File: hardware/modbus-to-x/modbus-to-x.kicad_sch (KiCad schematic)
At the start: 23 parts, among them SW1 SW_Push, SW2 SW_Push, U1 AMS1117-3.3, U2 LM7805_TO220, U3 MAX3485, U4 ESP32-WROOM-32D, U5 AT24CS64-XHM, U6 AT24CS64-XHM

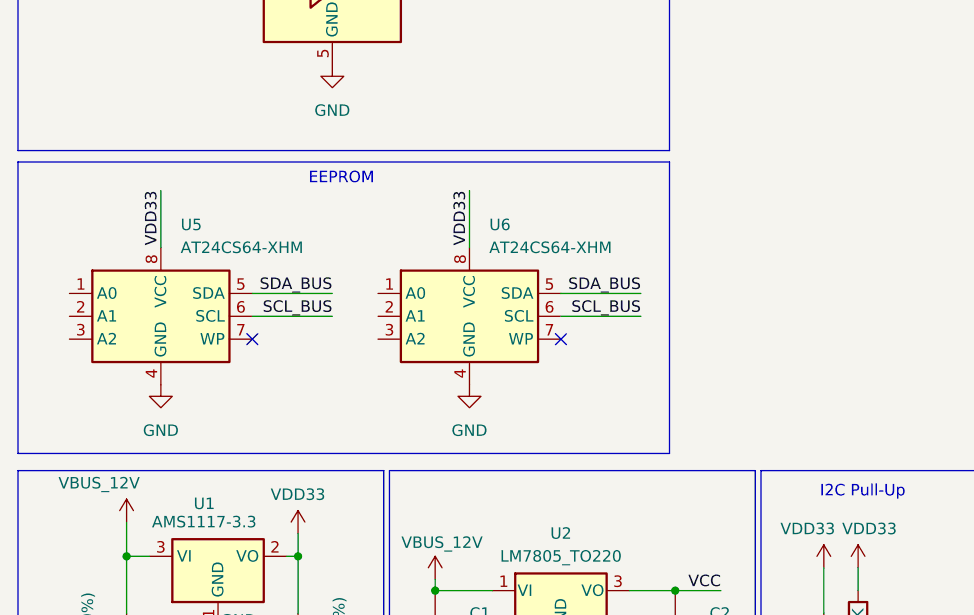
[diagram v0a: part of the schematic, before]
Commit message: hardwiring address pins in eeproms
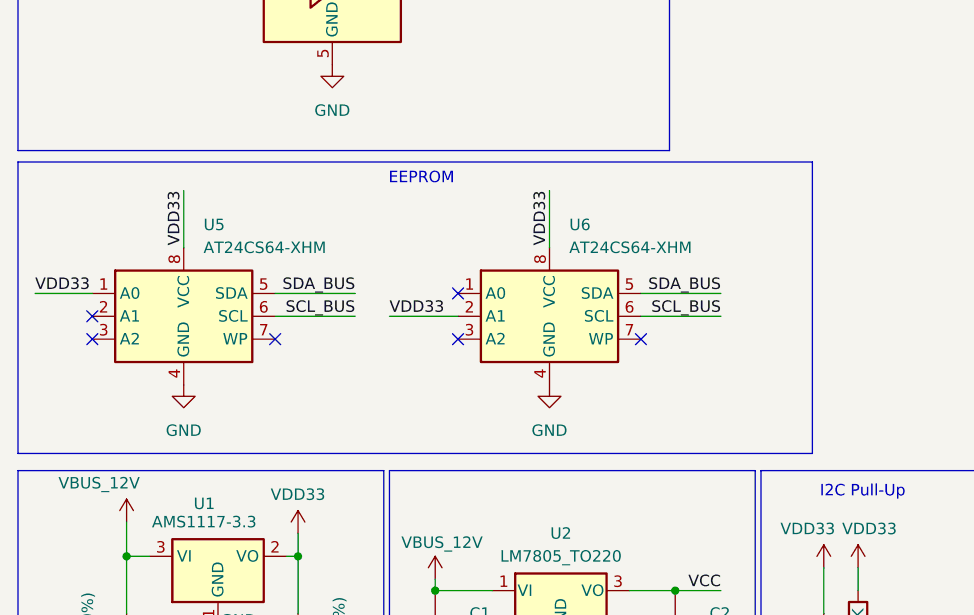
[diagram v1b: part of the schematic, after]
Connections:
- net VDD33: now also U5.1 (A0), U6.2 (A1)
- no-connect marks 10 -> 14
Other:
- moved on the sheet: U5, U6
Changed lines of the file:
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@@
 	)
 	(no_connect
-		(at 40.64 147.32)
+		(at 22.86 147.32)
+	)
+	(no_connect
+		(at 43.18 147.32)
 	)
 	(no_connect
@@
 	)
 	(no_connect
+		(at 22.86 144.78)
+	)
+	(no_connect
 		(at 240.03 72.39)
 	)
 	(no_connect
+		(at 63.5 147.32)
+	)
+	(no_connect
 		(at 240.03 77.47)
 	)
 	(no_connect
+		(at 63.5 142.24)
+	)
+	(no_connect
 		(at 240.03 69.85)
 	)
@@
 	)
 	(no_connect
-		(at 74.93 147.32)
+		(at 83.82 147.32)
 	)
 	(wire
@@
 	(wire
 		(pts
-			(xy 49.53 142.24) (xy 40.64 142.24)
+			(xy 52.07 142.24) (xy 43.18 142.24)
 		)
 		(stroke
@@
 	(wire
 		(pts
-			(xy 83.82 144.78) (xy 74.93 144.78)
+			(xy 92.71 144.78) (xy 83.82 144.78)
 		)
 		(stroke
@@
 	(wire
 		(pts
-			(xy 64.77 130.81) (xy 64.77 137.16)
+			(xy 73.66 130.81) (xy 73.66 137.16)
 		)
 		(stroke
@@
 	(wire
 		(pts
-			(xy 30.48 130.81) (xy 30.48 137.16)
+			(xy 33.02 130.81) (xy 33.02 137.16)
 		)
 		(stroke
@@
 	(wire
 		(pts
+			(xy 55.88 144.78) (xy 63.5 144.78)
+		)
+		(stroke
+			(width 0)
+			(type default)
+		)
+	)
+	(wire
+		(pts
 			(xy 198.12 102.87) (xy 198.12 97.79)
 		)
@@
 	(wire
 		(pts
-			(xy 49.53 144.78) (xy 40.64 144.78)
+			(xy 52.07 144.78) (xy 43.18 144.78)
 		)
 		(stroke
@@
 	(wire
 		(pts
-			(xy 83.82 142.24) (xy 74.93 142.24)
+			(xy 92.71 142.24) (xy 83.82 142.24)
 		)
 		(stroke
@@
 		)
 	)
+	(wire
+		(pts
+			(xy 16.51 142.24) (xy 22.86 142.24)
+		)
+		(stroke
+			(width 0)
+			(type default)
+		)
+	)
 	(rectangle
 		(start 152.4 12.7)
@@
 	(rectangle
 		(start 14.605 127.635)
-		(end 86.995 160.02)
+		(end 102.87 160.02)
 		(stroke
 			(width 0)
@@
 	(text "EEPROM\n"
 		(exclude_from_sim no)
-		(at 50.546 129.54 0)
+		(at 59.436 129.54 0)
 		(effects
 			(font
@@
 	)
 	(label "VDD33"
-		(at 30.48 130.81 270)
+		(at 33.02 130.81 270)
 		(fields_autoplaced yes)
 		(effects
@@
 	)
 	(label "SCL_BUS"
-		(at 83.82 144.78 180)
+		(at 92.71 144.78 180)
 		(fields_autoplaced yes)
 		(effects
@@
 	)
 	(label "SCL_BUS"
-		(at 49.53 144.78 180)
+		(at 52.07 144.78 180)
 		(fields_autoplaced yes)
 		(effects
@@
 	)
 	(label "SDA_BUS"
-		(at 83.82 142.24 180)
+		(at 92.71 142.24 180)
 		(fields_autoplaced yes)
 		(effects
@@
 	)
 	(label "VDD33"
-		(at 64.77 130.81 270)
+		(at 73.66 130.81 270)
 		(fields_autoplaced yes)
 		(effects
@@
 	)
 	(label "SDA_BUS"
-		(at 49.53 142.24 180)
+		(at 52.07 142.24 180)
 		(fields_autoplaced yes)
 		(effects
@@
 		)
 	)
+	(label "VDD33"
+		(at 55.88 144.78 0)
+		(fields_autoplaced yes)
+		(effects
+			(font
+				(size 1.27 1.27)
+			)
+			(justify left bottom)
+		)
+	)
+	(label "VDD33"
+		(at 16.51 142.24 0)
+		(fields_autoplaced yes)
+		(effects
+			(font
+				(size 1.27 1.27)
+			)
+			(justify left bottom)
+		)
+	)
 	(label "RS485_RE"
 		(at 27.94 99.06 0)
@@
 	(symbol
 		(lib_id "power:GND")
-		(at 64.77 152.4 0)
+		(at 73.66 152.4 0)
 		(unit 1)
 		(exclude_from_sim no)
@@
 		(fields_autoplaced yes)
 		(property "Reference" "#PWR019"
-			(at 64.77 158.75 0)
+			(at 73.66 158.75 0)
 			(effects
 				(font
@@
 		)
 		(property "Value" "GND"
-			(at 64.77 157.48 0)
+			(at 73.66 157.48 0)
 			(effects
 				(font
@@
 		)
 		(property "Footprint" ""
-			(at 64.77 152.4 0)
+			(at 73.66 152.4 0)
 			(effects
 				(font
@@
 		)
 		(property "Datasheet" ""
-			(at 64.77 152.4 0)
+			(at 73.66 152.4 0)
 			(effects
 				(font
@@
 		)
 		(property "Description" "Power symbol creates a global label with name \"GND\" , ground"
-			(at 64.77 152.4 0)
+			(at 73.66 152.4 0)
 			(effects
 				(font
@@
 	(symbol
 		(lib_id "power:GND")
-		(at 30.48 152.4 0)
+		(at 33.02 152.4 0)
 		(unit 1)
 		(exclude_from_sim no)
@@
 		(fields_autoplaced yes)
 		(property "Reference" "#PWR018"
-			(at 30.48 158.75 0)
+			(at 33.02 158.75 0)
 			(effects
 				(font
@@
 		)
 		(property "Value" "GND"
-			(at 30.48 157.48 0)
+			(at 33.02 157.48 0)
 			(effects
 				(font
@@
 		)
 		(property "Footprint" ""
-			(at 30.48 152.4 0)
+			(at 33.02 152.4 0)
 			(effects
 				(font
@@
 		)
 		(property "Datasheet" ""
-			(at 30.48 152.4 0)
+			(at 33.02 152.4 0)
 			(effects
 				(font
@@
 		)
 		(property "Description" "Power symbol creates a global label with name \"GND\" , ground"
-			(at 30.48 152.4 0)
+			(at 33.02 152.4 0)
 			(effects
 				(font
@@
 	(symbol
 		(lib_id "Memory_EEPROM:AT24CS64-XHM")
-		(at 30.48 144.78 0)
+		(at 33.02 144.78 0)
 		(unit 1)
 		(exclude_from_sim no)
@@
 		(fields_autoplaced yes)
 		(property "Reference" "U5"
-			(at 32.6741 134.62 0)
+			(at 35.2141 134.62 0)
 			(effects
 				(font
@@
 		)
 		(property "Value" "AT24CS64-XHM"
-			(at 32.6741 137.16 0)
+			(at 35.2141 137.16 0)
 			(effects
 				(font
@@
 		)
 		(property "Footprint" "Package_SO:TSSOP-8_4.4x3mm_P0.65mm"
-			(at 30.48 144.78 0)
+			(at 33.02 144.78 0)
 			(effects
 				(font
@@
 		)
 		(property "Datasheet" "http://ww1.microchip.com/downloads/en/DeviceDoc/Atmel-8870-SEEPROM-AT24CS64-Datasheet.pdf"
-			(at 30.48 144.78 0)
+			(at 33.02 144.78 0)
 			(effects
 				(font
@@
 		)
 		(property "Description" "I2C Serial EEPROM, 64Kb (8192x8) with Unique Serial Number, TSSOP8"
-			(at 30.48 144.78 0)
+			(at 33.02 144.78 0)
 			(effects
 				(font
@@
 	(symbol
 		(lib_id "Memory_EEPROM:AT24CS64-XHM")
-		(at 64.77 144.78 0)
+		(at 73.66 144.78 0)
 		(unit 1)
 		(exclude_from_sim no)
@@
 		(fields_autoplaced yes)
 		(property "Reference" "U6"
-			(at 66.9641 134.62 0)
+			(at 75.8541 134.62 0)
 			(effects
 				(font
@@
 		)
 		(property "Value" "AT24CS64-XHM"
-			(at 66.9641 137.16 0)
+			(at 75.8541 137.16 0)
 			(effects
 				(font
@@
 		)
 		(property "Footprint" "Package_SO:TSSOP-8_4.4x3mm_P0.65mm"
-			(at 64.77 144.78 0)
+			(at 73.66 144.78 0)
 			(effects
 				(font
@@
 		)
 		(property "Datasheet" "http://ww1.microchip.com/downloads/en/DeviceDoc/Atmel-8870-SEEPROM-AT24CS64-Datasheet.pdf"
-			(at 64.77 144.78 0)
+			(at 73.66 144.78 0)
 			(effects
 				(font
@@
 		)
 		(property "Description" "I2C Serial EEPROM, 64Kb (8192x8) with Unique Serial Number, TSSOP8"
-			(at 64.77 144.78 0)
+			(at 73.66 144.78 0)
 			(effects
 				(font

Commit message: new power circuit WIP
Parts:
- added C10: 0.1uF, Capacitor_SMD:C_0402_1005Metric_Pad0.74x0.62mm_HandSolder, symbol Device:C
- added C11: 4.7uF, Capacitor_SMD:C_0402_1005Metric_Pad0.74x0.62mm_HandSolder, symbol Device:C
- added C12: 47uF, ~, symbol SparkFun-Capacitor:C_Polarized
- added D2: MBR0530, Diode_SMD:D_SOD-123, symbol Diode:MBR0530
- added L1: 5.5uH, SparkFun-Capacitor:C_0805_2012Metric, symbol SparkFun-Coil:L
- added R6, R8, R9: 10K, Resistor_SMD:R_0805_2012Metric_Pad1.20x1.40mm_HandSolder, symbol Device:R
- added R7: 23.2K, Resistor_SMD:R_0805_2012Metric_Pad1.20x1.40mm_HandSolder, symbol Device:R
- added U7: LMR14020SQDPRTQ1, DPR0010A, symbol LMR14020SQDPRTQ1:LMR14020SQDPRTQ1
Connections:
- net GND: now also C11.1, C12.2, D2.2 (A), R7.1, U7.11 (PAD), U7.9 (GND)
- net VBUS_12V: no longer C8.1, U1.3 (VI)
- net PGOOD: now reaches U4.16 (IO13)
- net PGOOD: now also R6.1
- new net: R6.2, U7.8 (PGOOD)
- new net: C10.2, U7.1 (BOOT)
- new net: D2.1 (K), L1.1, U7.10 (SW)
- new net: R7.2, U7.5 (RT_SYNC)
- new net: C11.2, U7.6 (SS)
- new net: R9.1, U7.7 (FB)
- new net: R8.2, R9.2
- new net VCC5: C12.1, C8.1, L1.2, R8.1, U1.3 (VI)

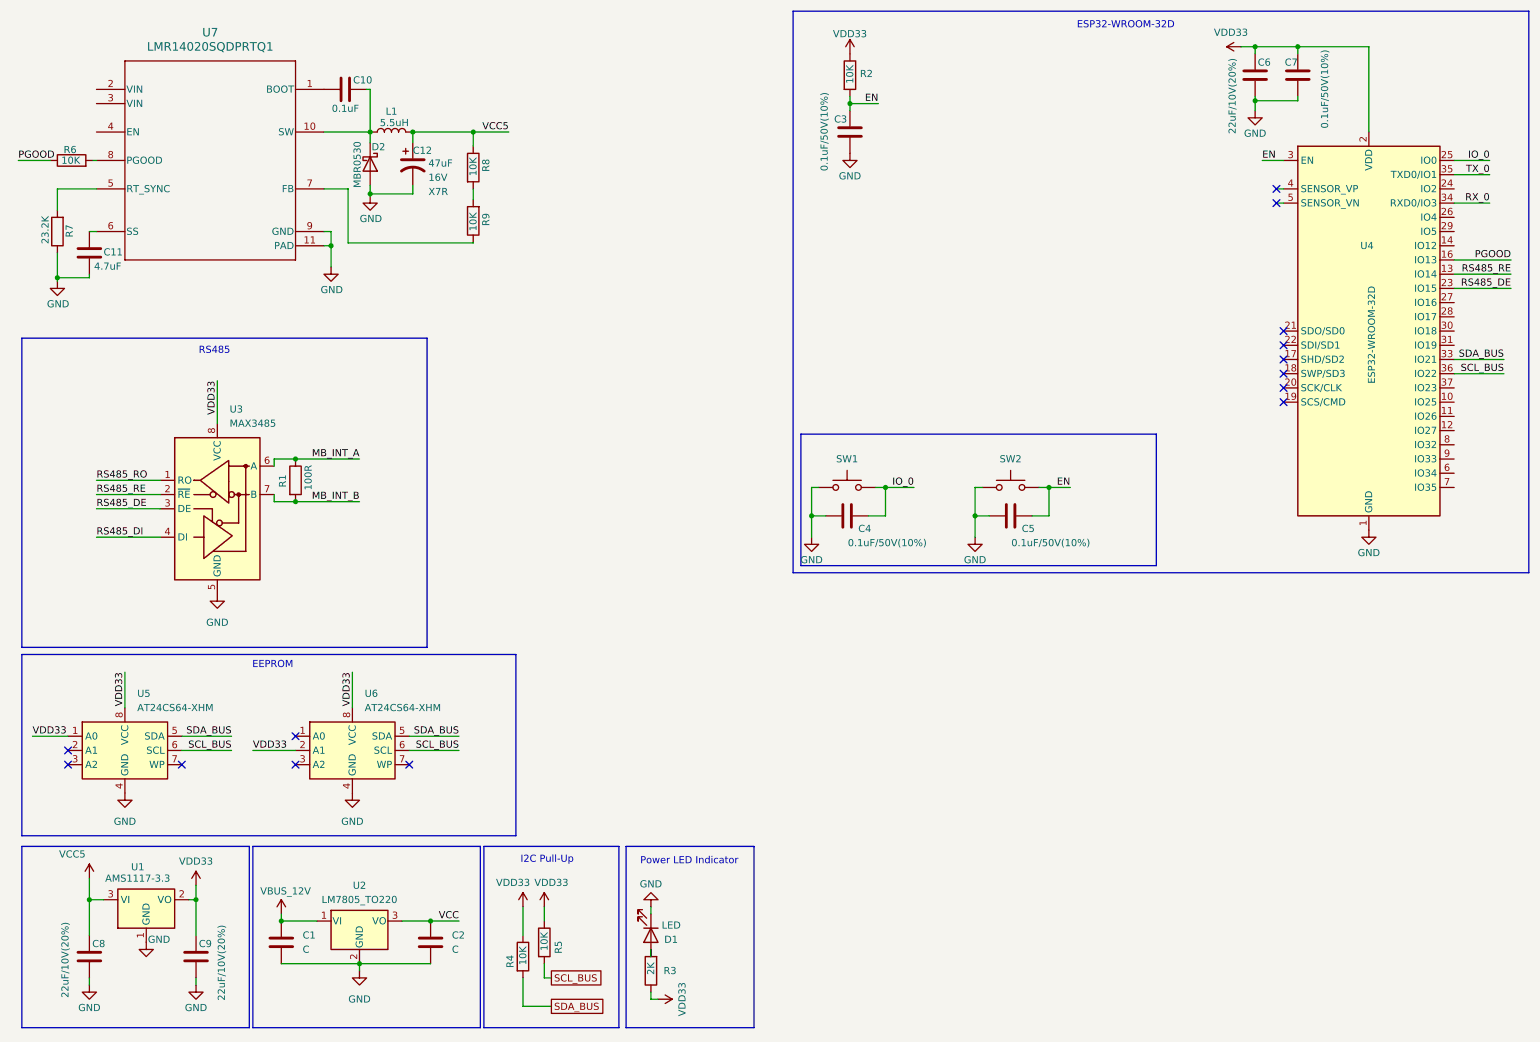
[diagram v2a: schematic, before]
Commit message: fixed warnings
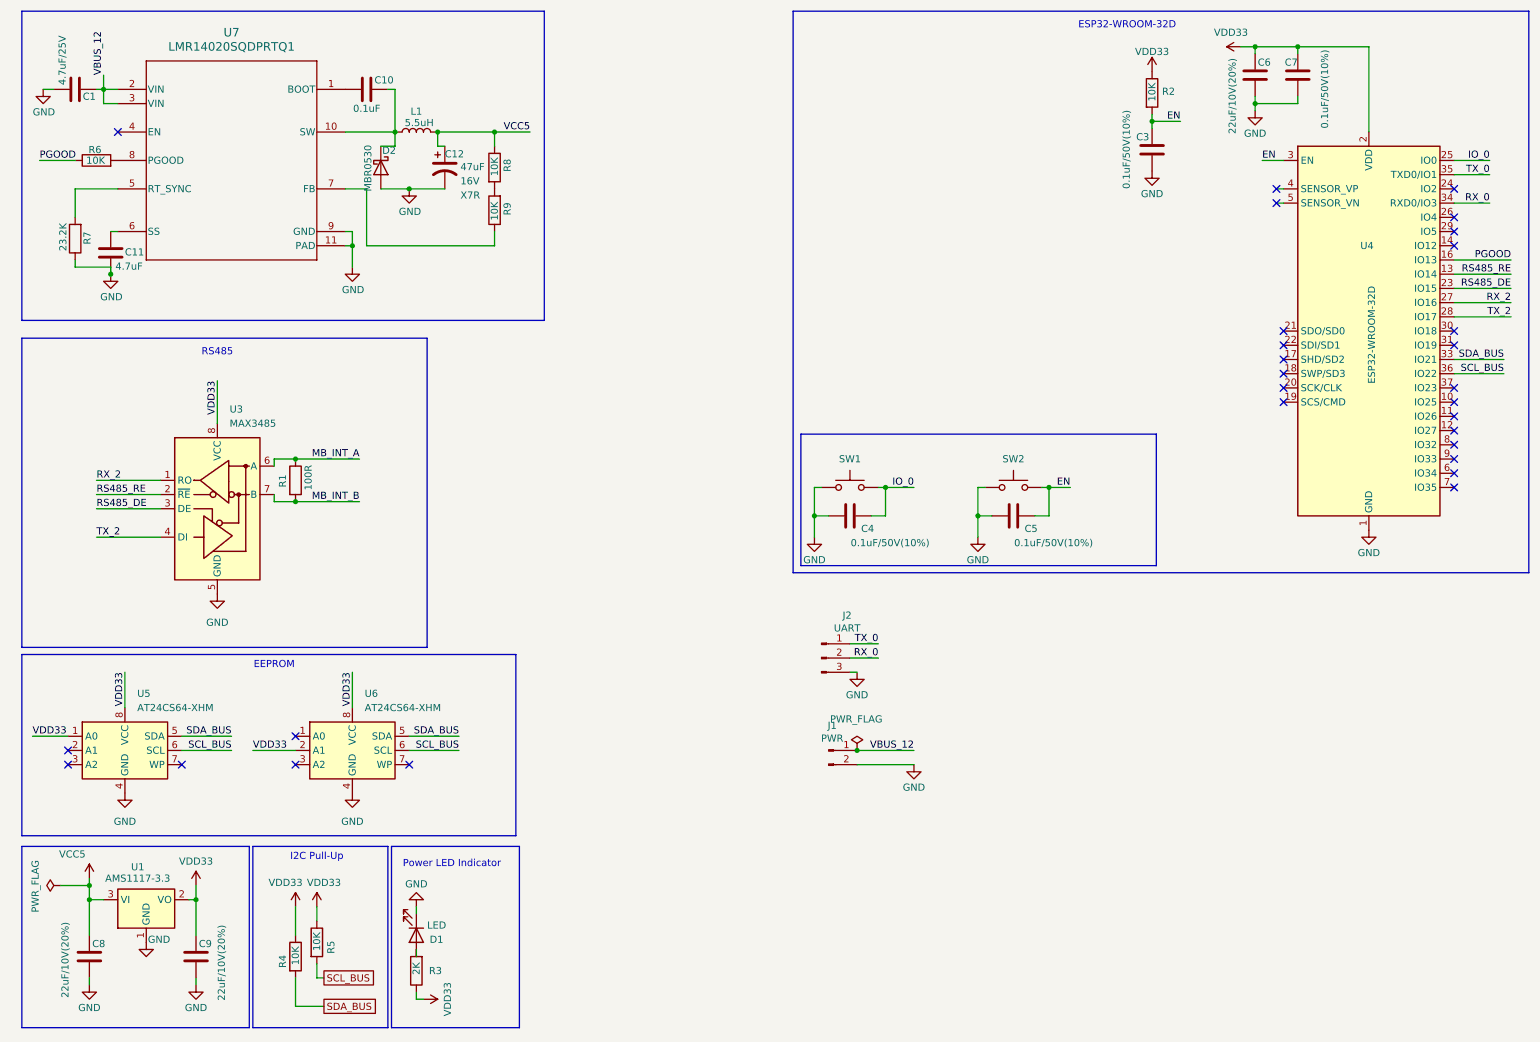
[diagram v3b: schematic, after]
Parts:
- removed C2: C, symbol Device:C
- removed U2: LM7805_TO220, Package_TO_SOT_THT:TO-220-3_Vertical, symbol Regulator_Linear:LM7805_TO220
- added J1: PWR, Connector_JST:JST_XH_B2B-XH-A_1x02_P2.50mm_Vertical, symbol Connector:Conn_01x02_Pin
- added J2: UART, Connector:FanPinHeader_1x03_P2.54mm_Vertical, symbol Connector:Conn_01x03_Pin
- C1: value C -> 4.7uF/25V
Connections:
- net RS485_DI is gone; now on net TX_2: U3.4 (DI)
- net RS485_RO is gone; now on net RX_2: U3.1 (RO)
- net VBUS_12V is gone; now on net GND: C1.1
- net GND: now also J1.2 (Pin_2), J2.3 (Pin_3); no longer C1.2
- net RX_0: now also J2.2 (Pin_2)
- net TX_0: now also J2.1 (Pin_1)
- net RX_2: now reaches U4.27 (IO16)
- net TX_2: now reaches U4.28 (IO17)
- net at D2.1 (K), L1.1, U7.10 (SW): now also C10.1
- net VBUS_12: now reaches U7.2 (VIN)
- net VBUS_12: now also C1.2, U7.3 (VIN), J1.1 (Pin_1)
- no-connect marks 14 -> 29
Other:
- moved on the sheet: C10, C11, C12, C3, C4, C5, D1, D2, L1, R2, R3, R4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

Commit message: fixed warnings
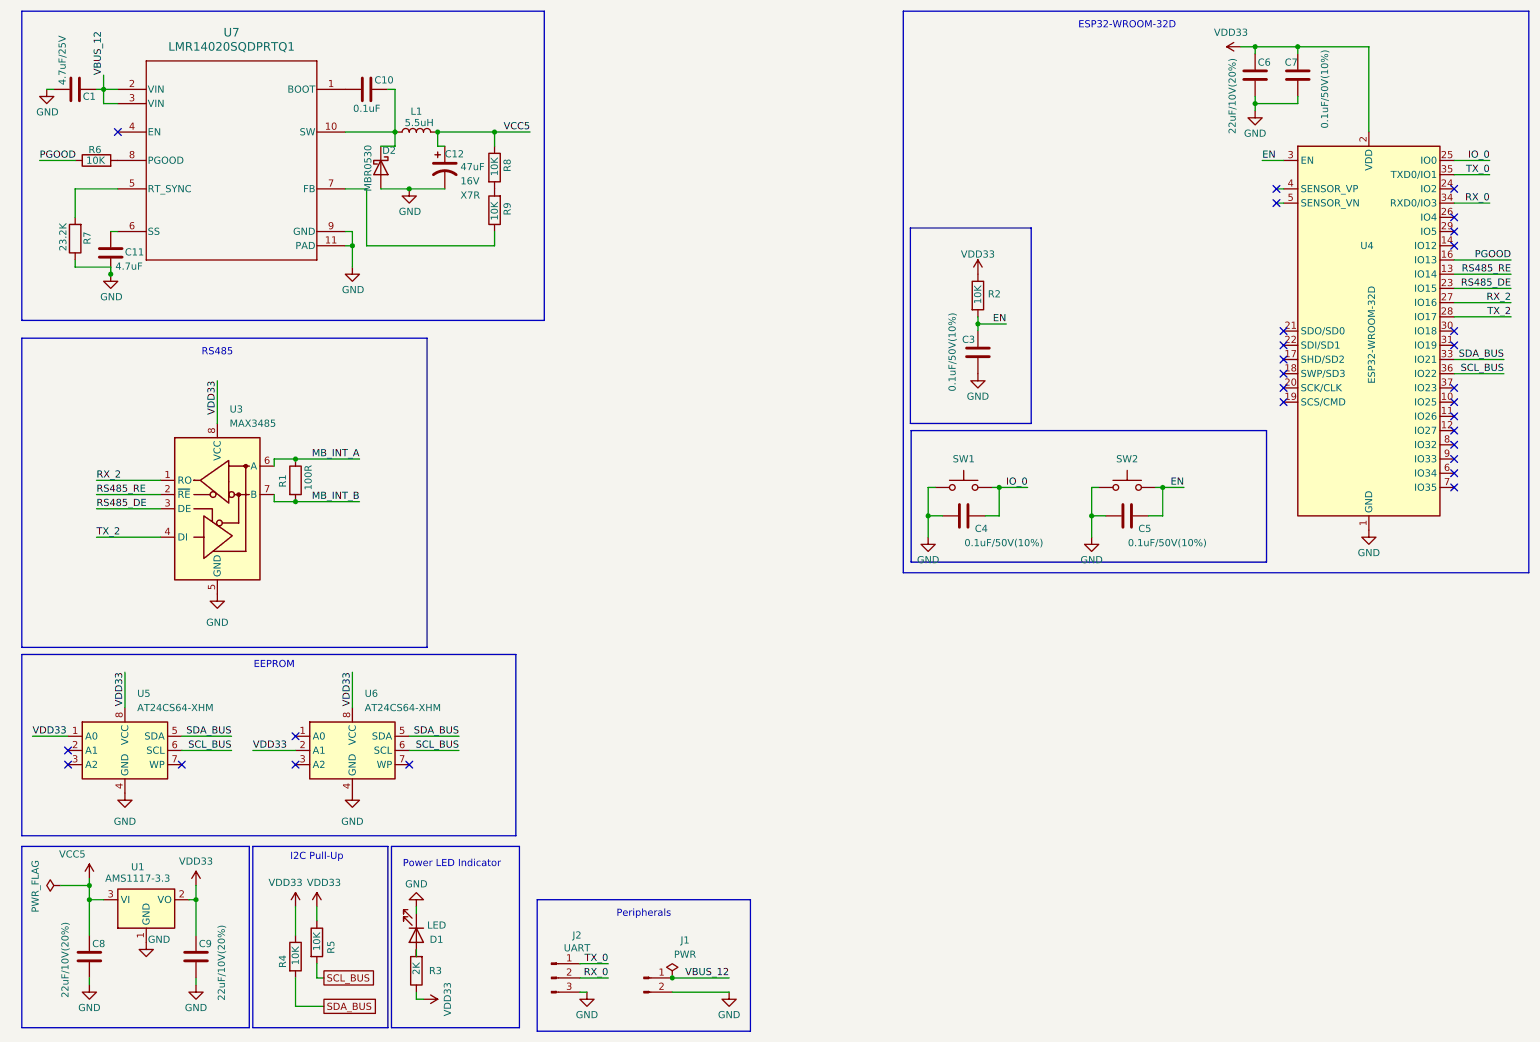
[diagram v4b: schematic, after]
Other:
- note added: "Peripherals"
- moved on the sheet: C3, C4, C5, J1, J2, R2, SW1, SW2
